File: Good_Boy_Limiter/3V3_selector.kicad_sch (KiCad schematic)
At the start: 10 parts, among them U5 SY8120B

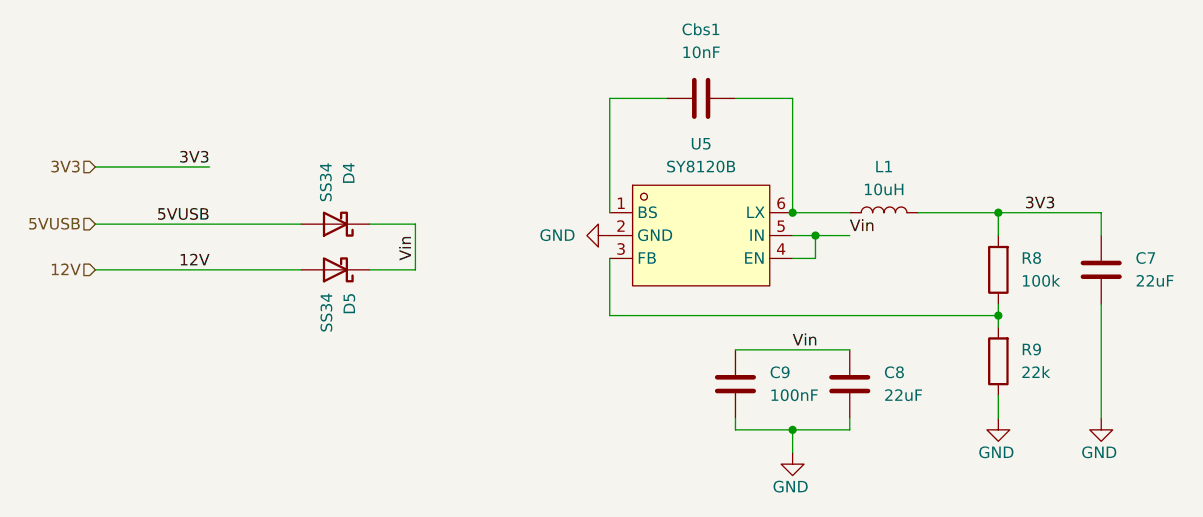
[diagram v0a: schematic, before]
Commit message: Added mounting holes and test points
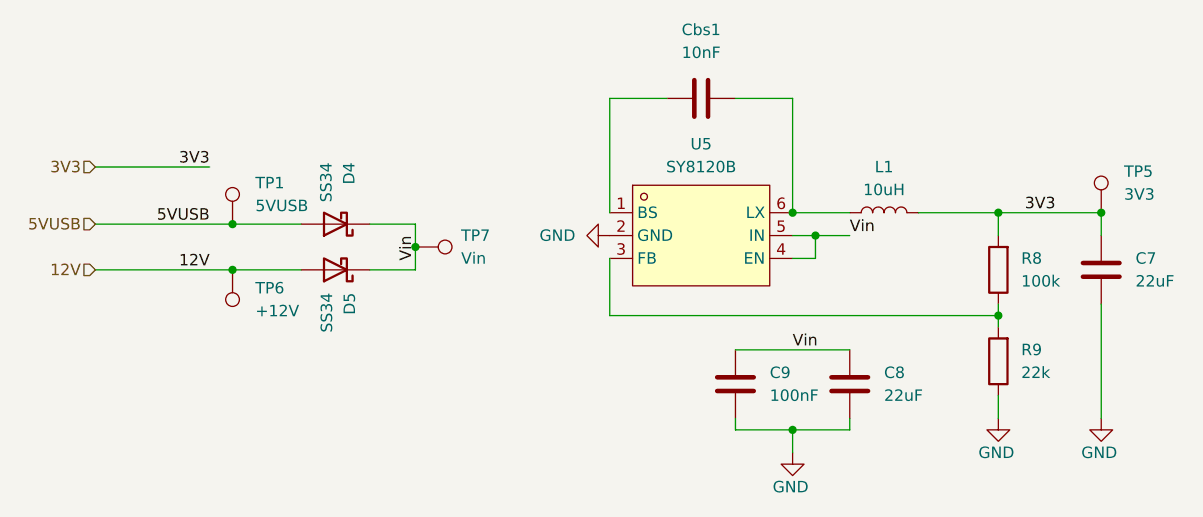
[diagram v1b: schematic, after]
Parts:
- added TP1: 5VUSB, TestPoint:TestPoint_Pad_D2.0mm, symbol Connector:TestPoint
- added TP5: 3V3, TestPoint:TestPoint_Pad_D2.0mm, symbol Connector:TestPoint
- added TP6: +12V, TestPoint:TestPoint_Pad_D2.0mm, symbol Connector:TestPoint
- added TP7: Vin, TestPoint:TestPoint_Pad_D2.0mm, symbol Connector:TestPoint
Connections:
- net 12V: now also TP6.1
- net 3V3: now also TP5.1
- net 5VUSB: now also TP1.1
- net Vin: now also TP7.1

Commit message: More update on routing
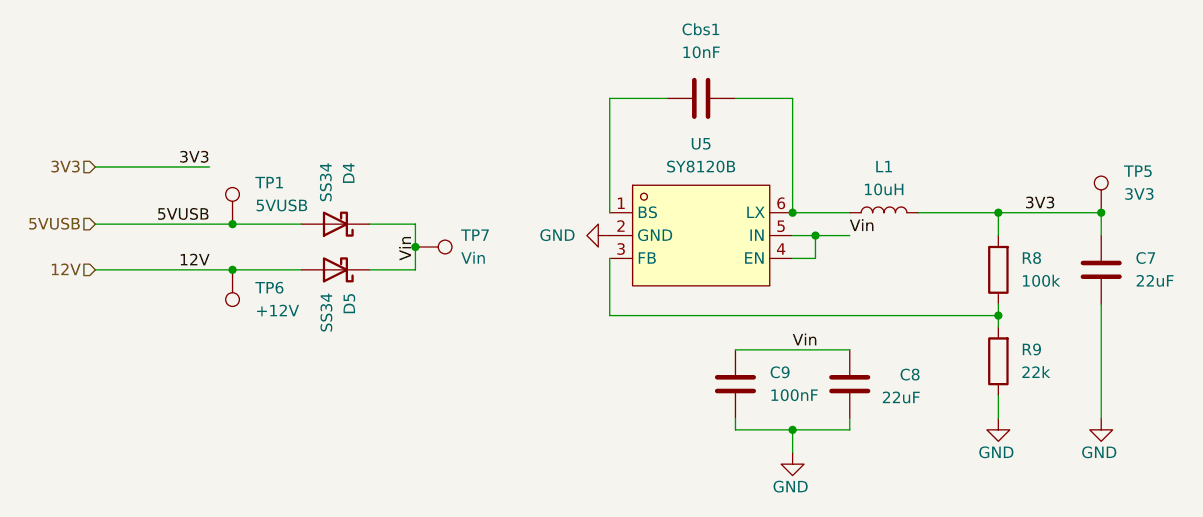
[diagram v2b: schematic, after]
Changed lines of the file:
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@@
 		(lib_id "Device:C")
 		(at 124.46 77.47 0)
+		(mirror y)
 		(unit 1)
 		(exclude_from_sim no)
@@
 		(on_board yes)
 		(dnp no)
-		(fields_autoplaced yes)
 		(property "Reference" "C8"
-			(at 128.27 76.1999 0)
+			(at 132.334 76.454 0)
 			(effects
 				(font
@@
 		)
 		(property "Value" "22uF"
-			(at 128.27 78.7399 0)
+			(at 132.334 78.994 0)
 			(effects
 				(font
@@
 		)
 		(property "Footprint" "Capacitor_SMD:C_1206_3216Metric_Pad1.33x1.80mm_HandSolder"
-			(at 125.4252 81.28 0)
+			(at 123.4948 81.28 0)
 			(effects
 				(font

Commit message: Added xt30 adn routed, ready for revision
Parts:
- TP7: footprint TestPoint:TestPoint_Pad_D2.0mm -> TestPoint:TestPoint_Pad_D1.5mm
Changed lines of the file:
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@@
 			)
 		)
-		(property "Footprint" "TestPoint:TestPoint_Pad_D2.0mm"
+		(property "Footprint" "TestPoint:TestPoint_Pad_D1.5mm"
 			(at 76.2 67.31 0)
 			(effects

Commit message: Finished e-scheme
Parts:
- R8: LCSC Part C177608 -> C25803
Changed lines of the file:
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@@
+			)
+		)
+		(property "Sim.Type" ""
+			(at 67.31 64.77 0)
+			(effects
+				(font
+					(size 1.27 1.27)
+				)
 			)
 		)
@@
 			)
 		)
+		(property "Sim.Type" ""
+			(at 107.95 60.96 0)
+			(effects
+				(font
+					(size 1.27 1.27)
+				)
+			)
+		)
 		(pin "1"
 		)
@@
 			)
 		)
+		(property "Sim.Type" ""
+			(at 140.97 74.93 0)
+			(effects
+				(font
+					(size 1.27 1.27)
+				)
+			)
+		)
 		(pin "2"
 		)
@@
 		)
 		(property "Sim.Device" ""
+			(at 67.31 59.69 0)
+			(effects
+				(font
+					(size 1.27 1.27)
+				)
+			)
+		)
+		(property "Sim.Type" ""
 			(at 67.31 59.69 0)
 			(effects
@@
 			)
 		)
+		(property "Sim.Type" ""
+			(at 152.4 58.42 0)
+			(effects
+				(font
+					(size 1.27 1.27)
+				)
+			)
+		)
 		(pin "1"
 		)
@@
 			)
 		)
+		(property "Sim.Type" ""
+			(at 76.2 62.23 0)
+			(effects
+				(font
+					(size 1.27 1.27)
+				)
+			)
+		)
 		(pin "1"
 		)
@@
 			)
 		)
+		(property "Sim.Type" ""
+			(at 124.46 77.47 0)
+			(effects
+				(font
+					(size 1.27 1.27)
+				)
+			)
+		)
 		(pin "1"
 		)
@@
 			)
 		)
+		(property "Sim.Type" ""
+			(at 107.95 45.72 0)
+			(effects
+				(font
+					(size 1.27 1.27)
+				)
+			)
+		)
 		(pin "1"
 		)
@@
 			)
 		)
+		(property "Sim.Type" ""
+			(at 55.88 59.69 0)
+			(effects
+				(font
+					(size 1.27 1.27)
+				)
+			)
+		)
 		(pin "1"
 		)
@@
 			)
 		)
+		(property "Sim.Type" ""
+			(at 152.4 64.77 0)
+			(effects
+				(font
+					(size 1.27 1.27)
+				)
+			)
+		)
 		(pin "1"
 		)
@@
 			)
 		)
+		(property "Sim.Type" ""
+			(at 111.76 77.47 0)
+			(effects
+				(font
+					(size 1.27 1.27)
+				)
+			)
+		)
 		(pin "1"
 		)
@@
 			)
 		)
-		(property "LCSC Part" "C177608"
+		(property "LCSC Part" "C25803"
 			(at 140.97 64.77 0)
 			(effects
@@
 				)
 				(hide yes)
+			)
+		)
+		(property "Sim.Type" ""
+			(at 140.97 64.77 0)
+			(effects
+				(font
+					(size 1.27 1.27)
+				)
 			)
 		)
@@
 			)
 		)
+		(property "Sim.Type" ""
+			(at 128.27 58.42 0)
+			(effects
+				(font
+					(size 1.27 1.27)
+				)
+			)
+		)
 		(pin "1"
 		)
@@
 			)
 		)
+		(property "Sim.Type" ""
+			(at 55.88 64.77 0)
+			(effects
+				(font
+					(size 1.27 1.27)
+				)
+			)
+		)

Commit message: started routing
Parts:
- TP5: footprint TestPoint:TestPoint_Pad_D2.0mm -> TestPoint:TestPoint_Pad_D1.0mm
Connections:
- net LX: now reaches Cbs1.2, L1.1, U5.6 (LX)
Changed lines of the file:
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@@
+		)
+	)
+	(label "LX"
+		(at 119.38 58.42 0)
+		(effects
+			(font
+				(size 1.27 1.27)
+			)
+			(justify left bottom)
 		)
 	)
@@
 			)
 		)
-		(property "Footprint" "TestPoint:TestPoint_Pad_D2.0mm"
+		(property "Footprint" "TestPoint:TestPoint_Pad_D1.0mm"
 			(at 157.48 58.42 0)
 			(effects

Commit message: routing finished
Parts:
- TP1: footprint TestPoint:TestPoint_Pad_D2.0mm -> TestPoint:TestPoint_Pad_D1.0mm
- TP7: footprint TestPoint:TestPoint_Pad_D1.5mm -> TestPoint:TestPoint_Pad_D1.0mm
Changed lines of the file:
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@@
 			)
 		)
-		(property "Footprint" "TestPoint:TestPoint_Pad_D1.5mm"
+		(property "Footprint" "TestPoint:TestPoint_Pad_D1.0mm"
 			(at 76.2 67.31 0)
 			(effects
@@
 			)
 		)
-		(property "Footprint" "TestPoint:TestPoint_Pad_D2.0mm"
+		(property "Footprint" "TestPoint:TestPoint_Pad_D1.0mm"
 			(at 60.96 59.69 0)
 			(effects
